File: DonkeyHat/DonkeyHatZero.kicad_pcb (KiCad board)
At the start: 2 copper layers, 66.2 x 29.2 mm, 12 parts, among them J1 GPIO, J2 Conn_01x02_Pin, J3 Conn_01x02_Pin, J5 Battery +, J6 Battery -, J7 +5v, J8 GND, U2 rp2040-zero

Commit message: Fixed spacing
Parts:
- moved RCin1 3.50 mm to (101.9, 51.2)
- moved J6 2.34 mm to (149.7, 54.5)
- moved J5 2.34 mm to (158.1, 54.5)
- moved U2 1.83 mm to (117.4, 61.3)
- moved J7 1.24 mm to (158.2, 69.2)
- moved J8 1.24 mm to (149.7, 69.2)
- moved Steer1 0.75 mm to (102.0, 66.2)
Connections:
- J7 pad : (no net) -> +5V
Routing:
- net GND: track 0.00 -> 86.1 mm
- net +5V: track 0.00 -> 82.4 mm, vias 0 -> 1
- net Rpi Rx: track 0.00 -> 62.0 mm
- net Rpi Tx: track 0.00 -> 59.6 mm
- net Steer: track 0.00 -> 41.7 mm
- net RCin1: track 0.00 -> 29.5 mm
- net Net-(J2-Pin_2): track 0.00 -> 27.3 mm
- net Net-(J2-Pin_1): track 0.00 -> 17.8 mm
- net Batt: track 0.00 -> 17.7 mm
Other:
- outline, holes or cut-outs redrawn
- board text added: "Steer"

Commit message: Updated zero
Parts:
- removed J5: Battery +, Connector_PinHeader_2.54mm:PinHeader_1x01_P2.54mm_Vertical
- removed J6: Battery -, Connector_PinHeader_2.54mm:PinHeader_1x01_P2.54mm_Vertical
- removed J7: +5v, Connector_PinHeader_2.54mm:PinHeader_1x01_P2.54mm_Vertical
- removed J8: GND, Connector_PinHeader_2.54mm:PinHeader_1x01_P2.54mm_Vertical
- removed the REF** at (103.2, 47.3)
- added ?: , , F.Cu at (147.9, 69.0)
- added ?: , , F.Cu at (156.3, 54.4)
- added ?: , , F.Cu at (147.9, 54.4)
- added ?: , , F.Cu at (156.4, 69.0)
- moved REF** 23.5 mm to (162.7, 70.8)
- moved Steer1 16.3 mm to (99.0, 50.2), turned to 90 degrees
- moved U2 7.73 mm to (109.9, 63.1)
- moved RCin1 5.81 mm to (99.0, 46.2), turned to 90 degrees
- moved J3 5.32 mm to (163.7, 61.7)
- moved J2 5.32 mm to (163.7, 51.5)
- moved J1 1.25 mm to (109.6, 49.1)
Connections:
- J2 pad 1: Net-(J2-Pin_1) -> Batt
- J2 pad 2: Net-(J2-Pin_2) -> GND
- J3 pad 1: Net-(J2-Pin_1) -> Batt
- J3 pad 2: Net-(J2-Pin_2) -> GND
- RCin1 pad 2: Batt -> Net-(RCin1-Pin_2)
- Steer1 pad 2: Batt -> Net-(RCin1-Pin_2)
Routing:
- net GND: track 86.1 -> 136.0 mm
- net Net-(J2-Pin_2): track 27.3 -> 0.00 mm
- net Net-(J2-Pin_1): track 17.8 -> 0.00 mm
- net RCin1: track 29.5 -> 15.4 mm, vias 0 -> 1
- net Steer: track 41.7 -> 33.1 mm, vias 0 -> 1
- net Net-(RCin1-Pin_2): track 0.00 -> 3.99 mm
- net Rpi Rx: track 62.0 -> 58.4 mm, vias 0 -> 1
- net Batt: track 17.7 -> 20.5 mm
- net +5V: track 82.4 -> 80.7 mm
- net Rpi Tx: track 59.6 -> 58.0 mm
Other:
- board size 66.2 x 29.2 mm -> 69.2 x 31.2 mm

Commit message: DFM tweaks
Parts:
- removed RCin1, Steer1: Conn_01x03_Pin, Connector_PinHeader_2.54mm:PinHeader_1x03_P2.54mm_Vertical
- added J4: Conn_02x03_Top_Bottom, Connector_PinHeader_2.54mm:PinHeader_2x03_P2.54mm_Vertical, F.Cu at (99.1, 49.5)
- moved ? 6.53 mm to (141.4, 69.8)
- moved ? 6.53 mm to (149.8, 55.1)
- moved ? 6.53 mm to (141.4, 55.1)
- moved ? 6.53 mm to (149.9, 69.8)
- moved J2 5.70 mm to (158.1, 52.8)
- moved J3 5.65 mm to (158.1, 62.1)
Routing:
- net +5V: track 80.7 -> 75.1 mm
- net Net-(RCin1-Pin_2): track 3.99 -> 0.00 mm
- net Net-(J4-Pin_2): track 0.00 -> 3.26 mm
- net GND: track 136.0 -> 133.6 mm
- net (no net): vias 0 -> 4

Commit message: Added latest prod version
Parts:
- removed J2, J3: Conn_01x02_Pin, Connector_PinHeader_2.54mm:PinHeader_1x02_P2.54mm_Vertical
- added ?: , , F.Cu at (160.4, 52.5)
- added ?: , , F.Cu at (160.4, 62.3)
- added ?: , , F.Cu at (160.5, 55.4)
- added ?: , , F.Cu at (160.5, 64.7)
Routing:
- net GND: track 133.6 -> 140.6 mm
- net Batt: track 20.5 -> 26.6 mm

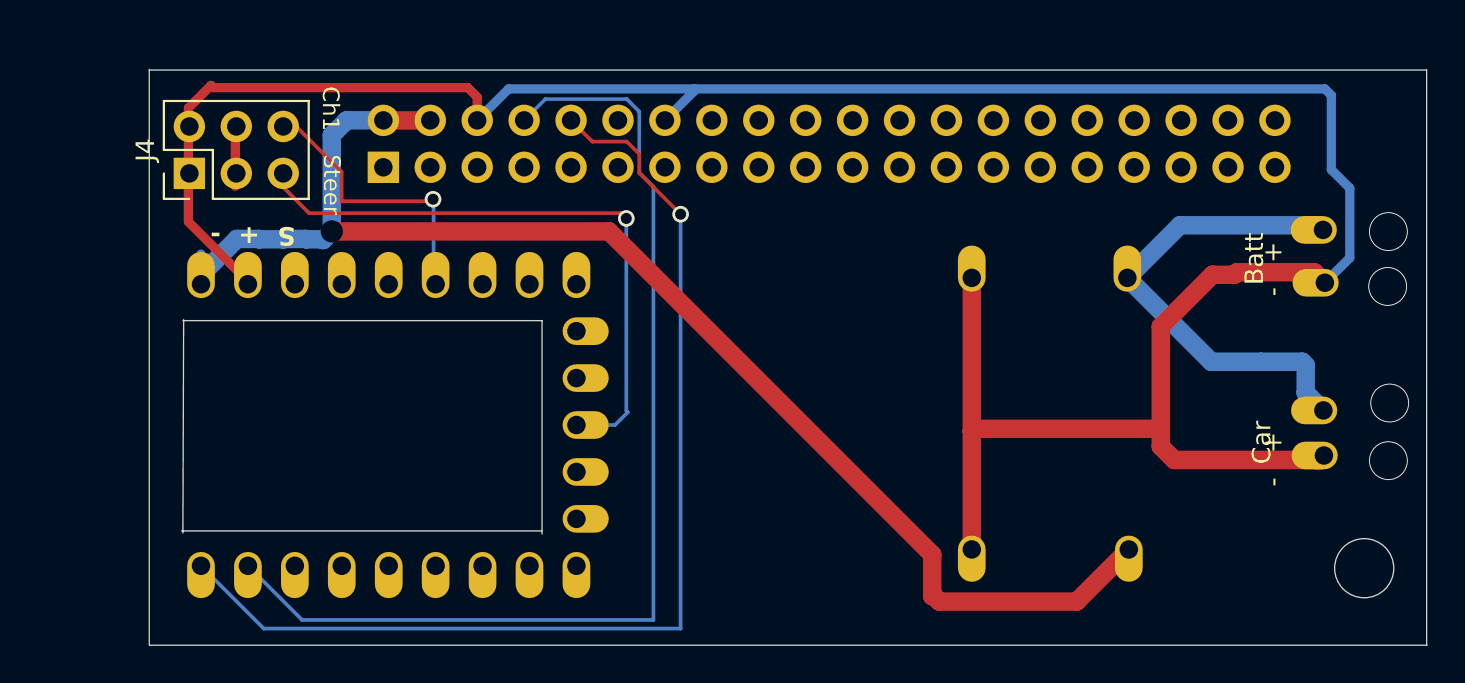
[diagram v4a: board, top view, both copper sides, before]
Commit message: Added OLED
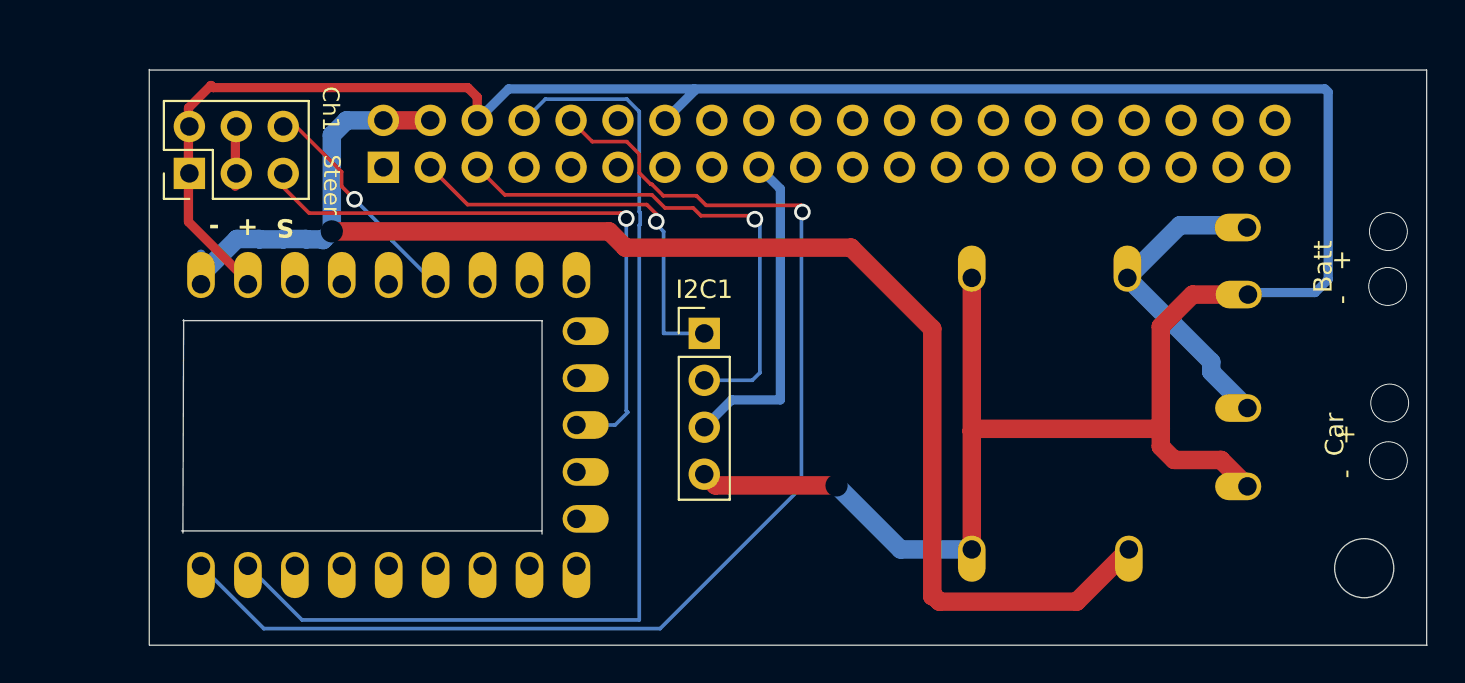
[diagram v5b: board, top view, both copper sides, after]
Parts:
- added I2C1: Conn_01x04_Pin, Connector_PinHeader_2.54mm:PinHeader_1x04_P2.54mm_Vertical, F.Cu at (126.9, 58.1)
- moved ? 4.46 mm to (156.3, 66.4)
- moved ? 4.21 mm to (156.4, 56.0)
- moved ? 4.11 mm to (156.3, 52.4)
- moved ? 4.11 mm to (156.3, 62.2)
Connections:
- J1 pad 1: unconnected-(J1-Pin_1-Pad1) -> +3V3
- J1 pad 17: unconnected-(J1-Pin_17-Pad17) -> +3V3
- J1 pad 3: unconnected-(J1-Pin_3-Pad3) -> /GPIO2/SDA1
- J1 pad 5: unconnected-(J1-Pin_5-Pad5) -> /GPIO3/SCL1
- U2 pad 17: unconnected-(U2-26-Pad17) -> RCin2
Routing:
- net /GPIO3/SCL1: track 0.00 -> 27.8 mm, vias 0 -> 1
- net /GPIO2/SDA1: track 0.00 -> 22.4 mm, vias 0 -> 1
- net +3V3: track 0.00 -> 17.8 mm
- net GND: track 140.6 -> 150.5 mm, vias 0 -> 1
- net Batt: track 26.6 -> 17.4 mm
- net Rpi Rx: track 58.4 -> 67.4 mm
- net +5V: track 75.1 -> 82.2 mm
- net RCin1: track 15.4 -> 12.8 mm
- net Rpi Tx: track 58.0 -> 56.9 mm

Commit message: Minor tweaks
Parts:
- moved I2C1 0.50 mm to (127.0, 57.6)
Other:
- board size 69.2 x 31.2 mm -> 69.1 x 30.8 mm
- board text added: "RC1"
- board text added: "RC2 In"
- board text added: "Thr"
- board text removed: "Ch1"
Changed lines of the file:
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@@
 	(footprint "Connector_PinHeader_2.54mm:PinHeader_1x04_P2.54mm_Vertical"
 		(layer "F.Cu")
-		(at 126.94 58.12)
+		(at 126.97 57.62)
 		(descr "Through hole straight pin header, 1x04, 2.54mm pitch, single row")
 		(tags "Through hole pin header THT 1x04 2.54mm single row")
@@
 	(gr_line
 		(start 96.9 43.833)
-		(end 96.9 74.967)
+		(end 96.96 74.63)
 		(stroke
 			(width 0.05)
@@
 	)
 	(gr_line
-		(start 166.04 75)
+		(start 166.04 74.64)
 		(end 166.04 43.866)
 		(stroke
@@
 	)
 	(gr_line
-		(start 96.9 74.997822)
-		(end 166.06 74.997822)
+		(start 96.96 74.64)
+		(end 166.04 74.64)
 		(stroke
 			(width 0.05)
@@
 		)
 		(layer "Edge.Cuts")
+	)
+	(gr_text "RC2 In"
+		(at 113.73 53.27 0)
+		(layer "F.SilkS")
+		(effects
+			(font
+				(size 0.5 0.5)
+				(thickness 0.1)
+			)
+			(justify left bottom)
+		)
 	)
 	(gr_text "Batt"
@@
 		)
 	)
+	(gr_text "Thr"
+		(at 122.15 65.99 0)
+		(layer "F.SilkS")
+		(effects
+			(font
+				(size 0.6 0.6)
+				(thickness 0.1)
+				(bold yes)
+			)
+			(justify left bottom)
+		)
+	)
 	(gr_text "-   +"
 		(at 162.02 56.54 90)
@@
 		)
 	)
-	(gr_text "Ch1"
-		(at 106.19 44.74 270)
+	(gr_text "RC1"
+		(at 106.26 45.18 270)
 		(layer "F.SilkS")
 		(effects
@@
 	)
 	(segment
-		(start 134.1 66.35)
-		(end 127.55 66.35)
-		(width 1)
-		(layer "F.Cu")
-		(net 1)
-	)
-	(segment
 		(start 99.020001 46.17)
 		(end 99.020001 45.919999)
@@
 	)
 	(segment
+		(start 134.1 66.35)
+		(end 128.02 66.35)
+		(width 1)
+		(layer "F.Cu")
+		(net 1)
+	)
+	(segment
 		(start 153.375 56.02)
 		(end 156.37 56.02)
@@
 	)
 	(segment
-		(start 127.55 66.35)
+		(start 127.12 65.92)
 		(end 126.94 65.74)
 		(width 1)
@@
 		(width 1)
 		(layer "F.Cu")
+		(net 1)
+	)
+	(segment
+		(start 127.59 65.92)
+		(end 127.12 65.92)
+		(width 1)
+		(layer "F.Cu")
+		(net 1)
+	)
+	(segment
+		(start 128.02 66.35)
+		(end 127.59 65.92)
+		(width 1)
+		(layer "F.Cu")
